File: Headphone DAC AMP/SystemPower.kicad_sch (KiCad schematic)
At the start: 12 parts, among them U1 NCV8187AMTW090TAG, U6 MCP1727-1802xSN, U7 MCP1727-3302xSN

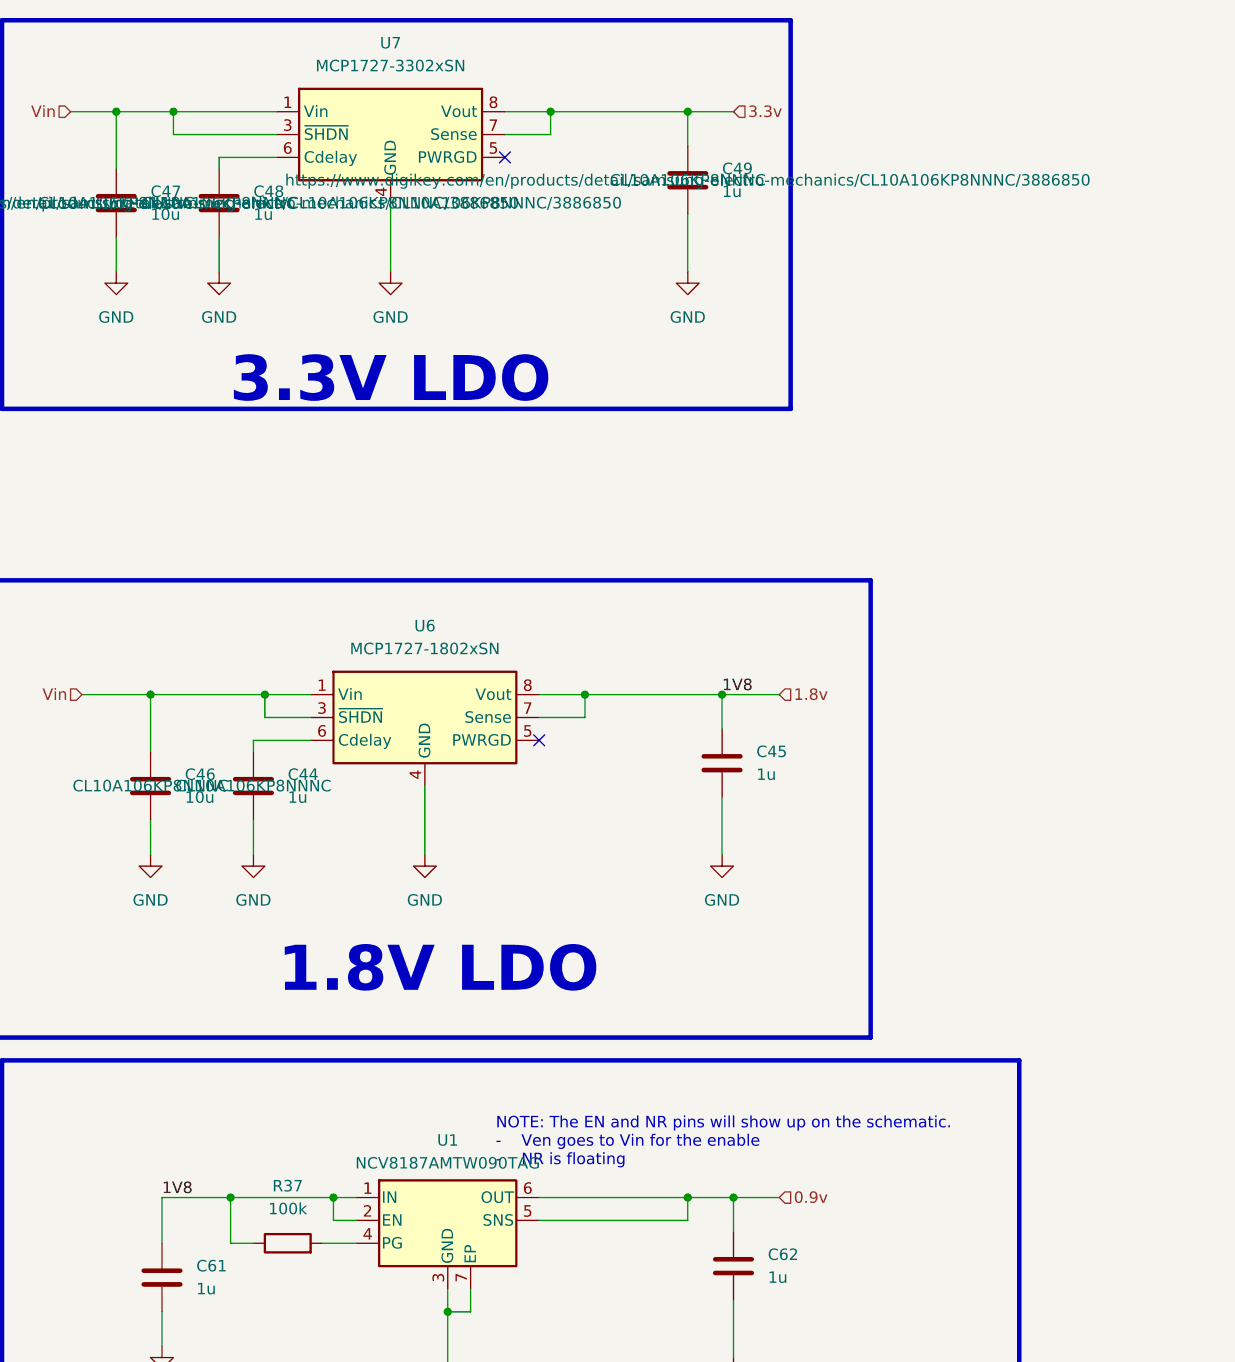
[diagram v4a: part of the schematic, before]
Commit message: Add TPS7A20 LDO regulator to SystemPower schematic
Added the TPS7A20xxxDQN linear regulator symbol and instance (U3) to the SystemPower.kicad_sch schematic, including relevant properties and pin definitions. Updated labels to reflect 3V3 output. Removed an old backup and added a new backup ZIP file.
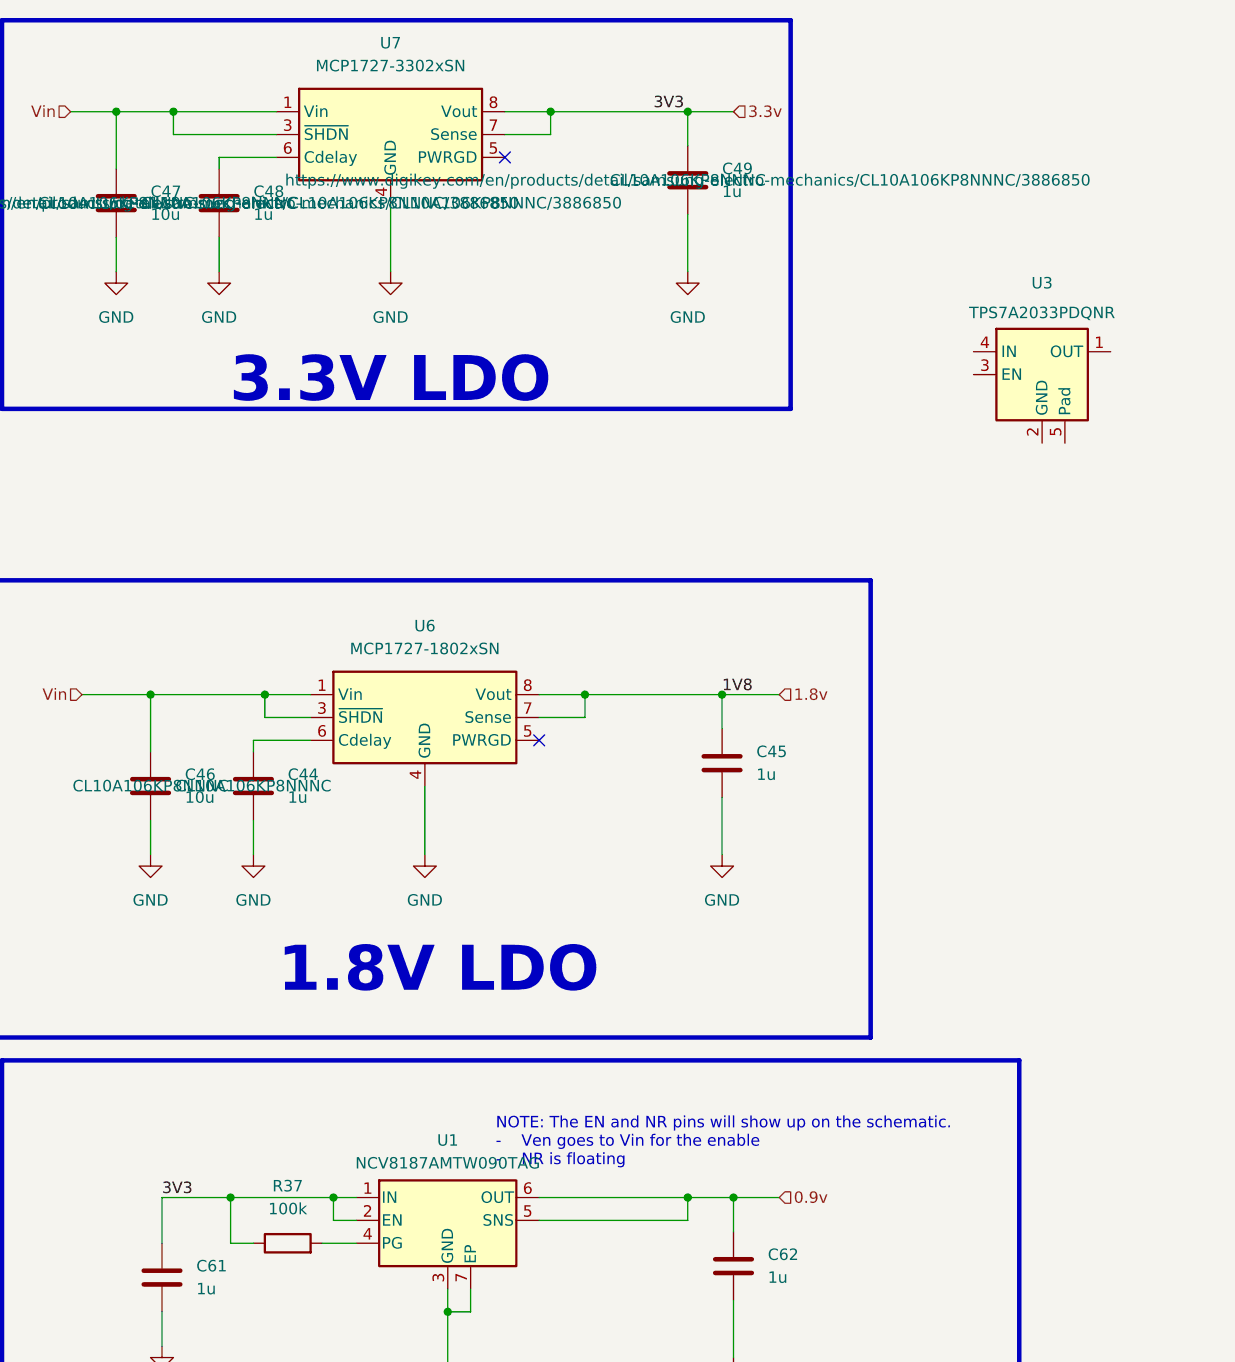
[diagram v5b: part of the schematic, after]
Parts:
- added U3: TPS7A20xxxDQN, Package_SON:Texas_X2SON-4_1x1mm_P0.65mm, symbol Regulator_Linear:TPS7A20xxxDQN
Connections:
- net 1.8v: no longer C61.1, R37.1, U1.1 (IN), U1.2 (EN), U1.6 (OUT)
- net 3.3v: now also C61.1, R37.1, U1.1 (IN), U1.2 (EN), U1.6 (OUT)
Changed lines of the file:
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@@
 		)
 	)
-	(label "1V8"
+	(label "3V3"
 		(at 40.64 148.59 0)
 		(effects
@@
 	(label "1V8"
 		(at 102.87 92.71 0)
+		(effects
+			(font
+				(size 1.27 1.27)
+			)
+			(justify left bottom)
+		)
+	)
+	(label "3V3"
+		(at 95.25 27.94 0)
 		(effects
 			(font
@@
 					(unit 1)
 				)
+			)
+		)
+	)
+	(symbol
+		(lib_id "Regulator_Linear:TPS7A20xxxDQN")
+		(at 138.43 57.15 0)
+		(unit 1)
+		(exclude_from_sim no)
+		(in_bom yes)
+		(on_board yes)
+		(dnp no)
+		(property "Reference" "U3"
+			(at 138.43 46.99 0)
+			(effects
+				(font
+					(size 1.27 1.27)
+				)
+			)
+		)
+		(property "Value" "TPS7A20xxxDQN"
+			(at 138.43 49.53 0)
+			(effects
+				(font
+					(size 1.27 1.27)
+				)
+				(hide yes)
+			)
+		)
+		(property "Footprint" "Package_SON:Texas_X2SON-4_1x1mm_P0.65mm"
+			(at 138.43 48.26 0)
+			(effects
+				(font
+					(size 1.27 1.27)
+				)
+				(hide yes)
+			)
+		)
+		(property "Datasheet" "https://www.ti.com/lit/ds/symlink/tps7a20.pdf"
+			(at 138.43 44.45 0)
+			(effects
+				(font
+					(size 1.27 1.27)
+				)
+				(hide yes)
+			)
+		)
+		(property "Description" "300 mA Low Dropout Voltage Regulator, Fixed Output, 1.6..6.0Vin, Low-Noise (7μV RMS), 6.5μA IQ LDO, X2SON-5"
+			(at 138.43 57.15 0)
+			(effects
+				(font
+					(size 1.27 1.27)
+				)
+				(hide yes)
+			)
+		)
+		(property "CUI_PURCHASE_URL" "https://www.digikey.com/en/products/detail/texas-instruments/TPS7A2033PDQNR/13245684"
+			(at 138.43 57.15 0)
+			(effects
+				(font
+					(size 1.27 1.27)
+				)
+				(hide yes)
+			)
+		)
+		(property "Mouser Part Number" "TPS7A2033PDQNR"
+			(at 138.43 50.292 0)
+			(effects
+				(font
+					(size 1.27 1.27)
+				)
+			)
+		)
+		(pin "1"
+		)
+		(pin "4"
+		)
+		(pin "3"
+		)
+		(pin "2"
+		)
+		(pin "5"
+		)
+		(instances
+			(project ""
+				(path "/d034eddd-efbc-47be-a25c-37cbfbab4cd8/a76b11f7-fbf9-4331-be15-052b46a69f96"
+					(reference "U3")
+					(unit 1)
+				)

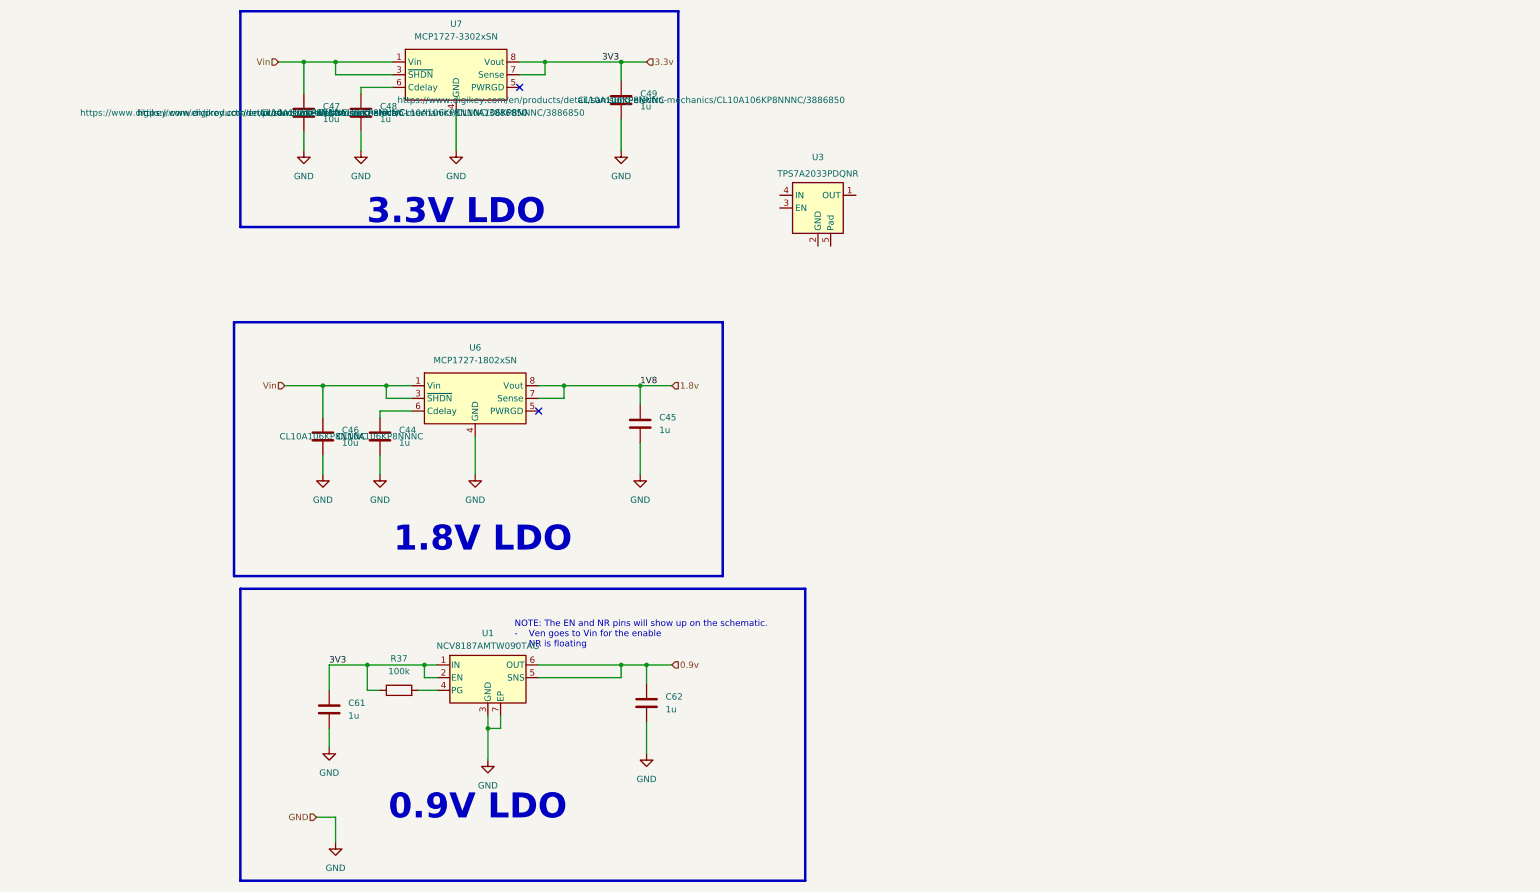
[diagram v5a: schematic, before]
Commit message: Worked on power schematic
planning to add debugging options
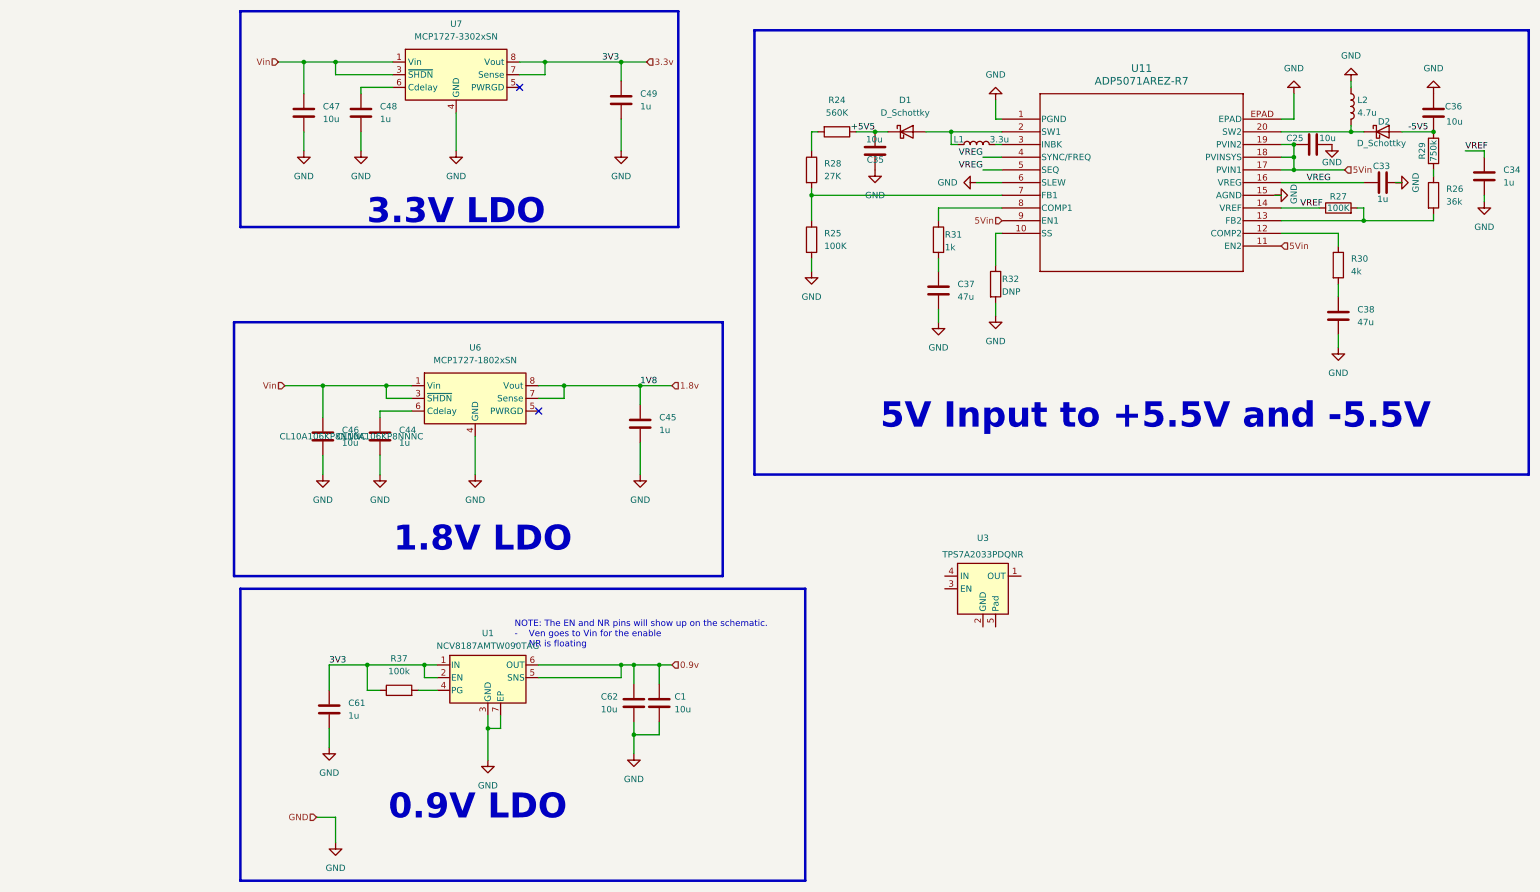
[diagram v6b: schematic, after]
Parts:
- added C1: 10u, Capacitor_SMD:C_0603_1608Metric, symbol Device:C
- added C25, C35, C36: 10u, Capacitor_SMD:C_0603_1608Metric_Pad1.08x0.95mm_HandSolder, symbol Device:C
- added C33, C34: 1u, Capacitor_SMD:C_0603_1608Metric_Pad1.08x0.95mm_HandSolder, symbol Device:C
- added C37, C38: 47u, Capacitor_SMD:C_0603_1608Metric_Pad1.08x0.95mm_HandSolder, symbol Device:C
- added D1, D2: D_Schottky, Capacitor_SMD:C_0603_1608Metric_Pad1.08x0.95mm_HandSolder, symbol Device:D_Schottky
- added L1: 3.3u, Inductor_SMD:L_0805_2012Metric, symbol Device:L
- added L2: 4.7u, Inductor_SMD:L_0805_2012Metric, symbol Device:L
- added R24: 560K, Resistor_SMD:R_0805_2012Metric_Pad1.20x1.40mm_HandSolder, symbol Device:R
- added R25, R27: 100K, Resistor_SMD:R_0805_2012Metric_Pad1.20x1.40mm_HandSolder, symbol Device:R
- added R26: 36k, Resistor_SMD:R_0805_2012Metric_Pad1.20x1.40mm_HandSolder, symbol Device:R
- added R28: 27K, Resistor_SMD:R_0805_2012Metric_Pad1.20x1.40mm_HandSolder, symbol Device:R
- added R29: 750k, Resistor_SMD:R_0805_2012Metric_Pad1.20x1.40mm_HandSolder, symbol Device:R
- added R30: 4k, Resistor_SMD:R_0805_2012Metric_Pad1.20x1.40mm_HandSolder, symbol Device:R
- added R31: 1k, Resistor_SMD:R_0805_2012Metric_Pad1.20x1.40mm_HandSolder, symbol Device:R
- added R32: DNP, Resistor_SMD:R_0805_2012Metric_Pad1.20x1.40mm_HandSolder, symbol Device:R
- added U11: ADP5071AREZ-R7, ADP5071:RE-20-1_ADI, symbol ADP5071AREZ-R7:ADP5071AREZ-R7
- C62: value 1u -> 10u
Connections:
- net 0.9v: now also C1.1
- net GND: now also C1.2, C25.1, C33.2, C34.2, C35.1, C36.1, C37.2, C38.2, L2.1, R25.2, R32.2, U11.1 (PGND), U11.15 (AGND), U11.6 (SLEW), U11.EPAD
- new net: C37.1, R31.2
- new net: R31.1, U11.8 (COMP1)
- new net: R26.2, R27.2, U11.13 (FB2)
- new net: R32.1, U11.10 (SS)
- new net: R30.1, U11.12 (COMP2)
- new net: D1.2 (A), L1.1, U11.2 (SW1)
- new net: D2.1 (K), L2.2, U11.20 (SW2)
- new net: L1.2, U11.3 (INBK)
- new net: R25.1, R28.2, U11.7 (FB1)
- new net: C38.1, R30.2
- new net: R26.1, R29.2
- new net: R24.2, R28.1
- new net +5V5: C35.2, D1.1 (K), R24.1
- new net -5V5: C36.2, D2.2 (A), R29.1
- new net 5Vin: C25.2, U11.11 (EN2), U11.17 (PVIN1), U11.18 (PVINSYS), U11.19 (PVIN2), U11.9 (EN1)
- new net VREF: C34.1, R27.1, U11.14 (VREF)
- new net VREG: C33.1, U11.16 (VREG), U11.4 (SYNC/FREQ), U11.5 (SEQ)
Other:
- note added: "5V Input to +5.5V and -5.5V"
- moved on the sheet: C62, U3
